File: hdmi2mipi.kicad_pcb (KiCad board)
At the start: 4 copper layers, 55 x 55 mm, 166 parts, among them J1 USB_C_Receptacle_USB2.0, J2 HDMI_A_1.4, J4 TP, J5 QWIIC, J6 BOOT, J7 SWD, J8 AudioJack3, J9 QWIIC, Q1 BC846, Q2 BC846, Q3 BC846, Q4 BC846, Q5 BC846, Q6 BC846, Q7 2SC2712, U1 SY8079AAC, U10 SY8079AAC, U11 SY8079AAC, U3 SY6280AAC, U4 PCA9306DC, U5 W25Q16JVUXIQ, U6 W25Q16JVUXIQ, U7 RP2040, U8 MS4344, U9 SY8079AAC, X1 SG-210STF, Y1 12MHz

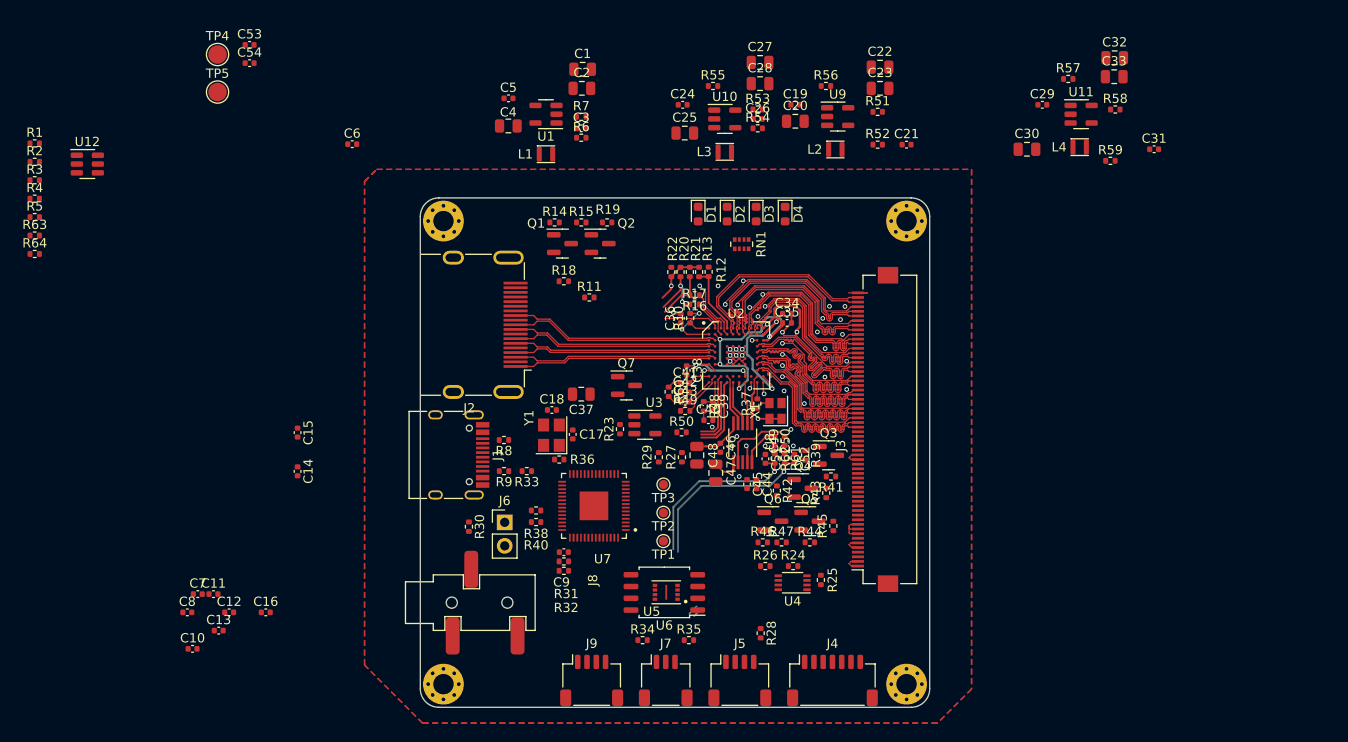
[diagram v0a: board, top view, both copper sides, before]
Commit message: Simplify and get ready for component placement and routing
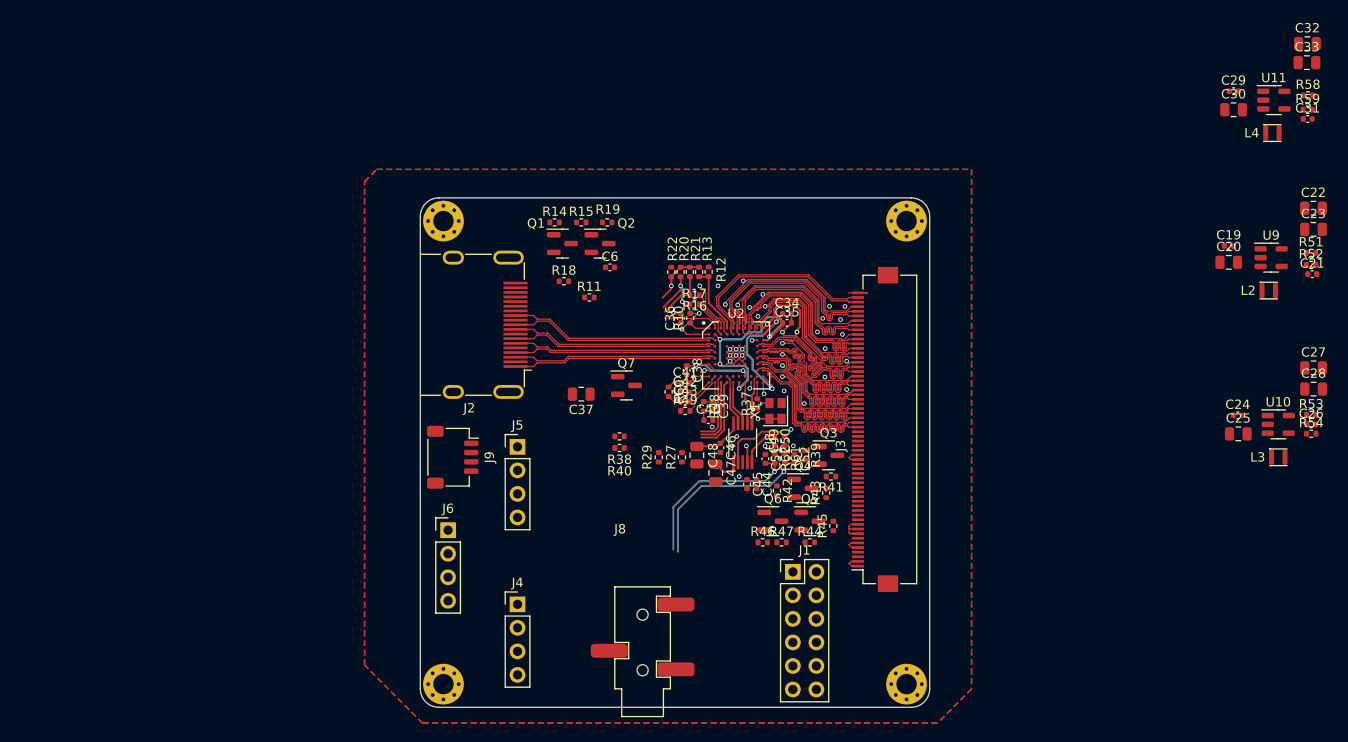
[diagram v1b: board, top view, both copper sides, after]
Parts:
- removed C1, C2, C4: 22u, Capacitor_SMD:C_0805_2012Metric
- removed C10, C12, C13, C14, C15, C16, C5, C7, C9: 100n, Capacitor_SMD:C_0402_1005Metric
- removed C11, C8: 1u, Capacitor_SMD:C_0402_1005Metric
- removed C17, C18, C3: 22p, Capacitor_SMD:C_0402_1005Metric
- removed C53: 2.2u, Capacitor_SMD:C_0402_1005Metric
- removed C54: ~, Capacitor_SMD:C_0402_1005Metric
- removed D1, D2, D3, D4: LED, LED_SMD:LED_0603_1608Metric
- removed J7: SWD, Connector_JST:JST_SH_SM03B-SRSS-TB_1x03-1MP_P1.00mm_Horizontal
- removed L1: 2.2u, custom:Inductor_MSC20FC
- removed R1, R50, R55, R56, R57, R7: 10k, Resistor_SMD:R_0402_1005Metric
- removed R2: 0, Resistor_SMD:R_0402_1005Metric
- removed R23, R24, R25, R26, R28: 4.7k, Resistor_SMD:R_0402_1005Metric
- removed R3, R4: 10, Resistor_SMD:R_0402_1005Metric
- removed R30, R33, R36: 1k, Resistor_SMD:R_0402_1005Metric
- removed R31, R32: 27, Resistor_SMD:R_0402_1005Metric
- removed R34, R35: 100, Resistor_SMD:R_0402_1005Metric
- removed R5: 6.8k, Resistor_SMD:R_0402_1005Metric
- removed R6: 45.3k, Resistor_SMD:R_0402_1005Metric
- removed R63: 50k, Resistor_SMD:R_0402_1005Metric
- removed R64: 100k, Resistor_SMD:R_0402_1005Metric
- removed R8, R9: 5.1k, Resistor_SMD:R_0402_1005Metric
- removed RN1: 1K, Resistor_SMD:R_Array_Convex_4x0402
- removed TP1, TP2, TP3: TestPoint, TestPoint:TestPoint_Pad_D1.0mm
- removed TP4, TP5: TestPoint, TestPoint:TestPoint_Pad_D2.0mm
- removed U1: SY8079AAC, Package_TO_SOT_SMD:SOT-23-5
- removed U12: ~, Package_TO_SOT_SMD:SOT-23-6
- removed U3: SY6280AAC, Package_TO_SOT_SMD:SOT-23-5
- removed U4: PCA9306DC, Package_SO:VSSOP-8_2.3x2mm_P0.5mm
- removed U5: W25Q16JVUXIQ, custom:PSON50P300X200X60-9N
- removed U6: W25Q16JVUXIQ, Package_SO:SOIC-8_5.23x5.23mm_P1.27mm
- removed U7: RP2040, custom:QFN40P700X700X90-57N
- removed Y1: 12MHz, Crystal:Crystal_SMD_3225-4Pin_3.2x2.5mm
- C6: value ~ -> 0.1u
- J1: value USB_C_Receptacle_USB2.0 -> IO; footprint Connector_USB:USB_C_Receptacle_HRO_TYPE-C-31-M-12 -> Connector_PinHeader_2.54mm:PinHeader_2x06_P2.54mm_Vertical
- J4: value TP -> Conn_01x04; footprint Connector_JST:JST_SH_SM07B-SRSS-TB_1x07-1MP_P1.00mm_Horizontal -> Connector_PinHeader_2.54mm:PinHeader_1x04_P2.54mm_Vertical
- J5: value QWIIC -> Conn_01x04; footprint Connector_JST:JST_SH_SM04B-SRSS-TB_1x04-1MP_P1.00mm_Horizontal -> Connector_PinHeader_2.54mm:PinHeader_1x04_P2.54mm_Vertical
- J6: value BOOT -> Conn_01x03; footprint Connector_PinHeader_2.54mm:PinHeader_1x02_P2.54mm_Vertical -> Connector_PinHeader_2.54mm:PinHeader_1x04_P2.54mm_Vertical
- moved C24 68.7 mm to (60.8, -4.02)
- moved C27 68.3 mm to (68.9, -9.15)
- moved C28 68.3 mm to (68.9, -6.86)
- moved C26 68.3 mm to (68.7, -3.05)
- moved L3 68.3 mm to (65.1, 0.51)
- moved R53 68.3 mm to (68.7, -4.07)
- moved R54 68.3 mm to (68.7, -2.03)
- moved U10 68.3 mm to (65.1, -3.05)
- moved C25 68.0 mm to (60.8, -2.02)
- moved L2 49.2 mm to (64.1, -17.5)
- moved C19 49.2 mm to (59.8, -22.3)
- moved C20 49.2 mm to (59.8, -20.5)
- moved C22 49.2 mm to (68.9, -26.4)
- moved C23 49.2 mm to (68.9, -24.1)
- moved R51 49.2 mm to (68.7, -21.6)
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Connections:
- C19 pad 1: VBUS -> 3V3_HDMI
- C20 pad 1: VBUS -> 3V3_HDMI
- C24 pad 1: VBUS -> 3V3_HDMI
- C25 pad 1: VBUS -> 3V3_HDMI
- C29 pad 1: VBUS -> 3V3_HDMI
- C30 pad 1: VBUS -> 3V3_HDMI
- C44 pad 1: +3V3 -> 3V3_HDMI
- C45 pad 1: +3V3 -> 3V3_HDMI
- J3 pad 1: Net-(J3-FB1-Pad1) -> Net-(J1-Pin_4)
- J3 pad 10: Net-(D5-K) -> Net-(J1-Pin_8)
- J3 pad 13: Net-(J3-5.8v-VEE) -> Net-(J1-Pin_10)
- J3 pad 14: Net-(J3-5.8v-VDD) -> Net-(J1-Pin_12)
- J3 pad 2: Net-(J3-FB1-Pad1) -> Net-(J1-Pin_4)
- J3 pad 5: Net-(J3-FB2-Pad5) -> Net-(J1-Pin_6)
- J3 pad 6: Net-(J3-FB2-Pad5) -> Net-(J1-Pin_6)
- J3 pad 8: Net-(D5-K) -> Net-(J1-Pin_8)
- J3 pad 9: Net-(D5-K) -> Net-(J1-Pin_8)
- J4 pad 1: TP_INT -> GND
- J4 pad 2: TP_RST -> +1V1
- J4 pad 3: Net-(J4-Pin_3) -> +1V2
- J4 pad 4: Net-(J4-Pin_4) -> +1V8
- J5 pad 2: +3V3 -> 3V3_HDMI
- J6 pad 1: GND -> Net-(J6-Pin_1)
- J6 pad 2: /RP_BTN -> Net-(J6-Pin_2)
- J9 pad 2: +3V3 -> 3V3_HDMI
- J9 pad 3: Net-(J9-Pin_3) -> Net-(J5-Pin_3)
- J9 pad 4: Net-(J9-Pin_4) -> Net-(J5-Pin_4)
- R27 pad 2: Net-(J9-Pin_4) -> Net-(J5-Pin_4)
- R29 pad 2: Net-(J9-Pin_3) -> Net-(J5-Pin_3)
- R38 pad 1: Net-(U2-~{RESET}) -> 3V3_HDMI
- R38 pad 2: GND -> Net-(J6-Pin_2)
- R40 pad 1: Net-(U2-INT) -> Net-(J6-Pin_1)
- U10 pad 1: 1V1_EN -> 3V3_HDMI
- U10 pad 4: VBUS -> 3V3_HDMI
- U11 pad 1: 1V8_EN -> 3V3_HDMI
- U11 pad 4: VBUS -> 3V3_HDMI
- U2 pad J3: Net-(U2-INT) -> Net-(J6-Pin_1)
- U2 pad K3: Net-(J9-Pin_3) -> Net-(J5-Pin_3)
- U2 pad K4: Net-(J9-Pin_4) -> Net-(J5-Pin_4)
- U2 pad K8: Net-(U2-~{RESET}) -> Net-(J6-Pin_2)
- U8 pad 9: +3V3 -> 3V3_HDMI
- U9 pad 1: 1V2_EN -> 3V3_HDMI
- U9 pad 4: VBUS -> 3V3_HDMI
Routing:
- net Net-(J9-Pin_4): track 8.08 -> 0.00 mm
- net Net-(J5-Pin_4): track 0.00 -> 8.08 mm
- net Net-(U2-INT): track 7.68 -> 0.00 mm
- net Net-(J6-Pin_1): track 0.00 -> 7.68 mm
- net Net-(J9-Pin_3): track 7.41 -> 0.00 mm
- net Net-(J5-Pin_3): track 0.00 -> 7.41 mm
- net Net-(J1-Pin_8): track 0.00 -> 3.77 mm
- net Net-(D5-K): track 3.77 -> 0.00 mm
- net Net-(J3-FB2-Pad5): track 2.12 -> 0.00 mm
- net Net-(J3-FB1-Pad1): track 2.12 -> 0.00 mm
- net Net-(J1-Pin_6): track 0.00 -> 2.12 mm
- net Net-(J1-Pin_4): track 0.00 -> 2.12 mm
- net +3V3: track 1.81 -> 0.00 mm, vias 1 -> 0
- net 3V3_HDMI: track 21.8 -> 23.6 mm, vias 5 -> 6
- net /AUDIO_L: track 20.8 -> 19.7 mm
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- added copper zone on In2.Cu, net 3V3_HDMI
- removed copper zone on In2.Cu, net +3V3

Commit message: tracing done
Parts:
- moved C33 86.3 mm to (1.20, 12.2), turned to -90 degrees
- moved C32 82.4 mm to (6.20, 9.98), turned to -90 degrees
- moved C28 79.5 mm to (-9.72, 4.44), turned to 90 degrees
- moved C30 78.5 mm to (-0.84, 12.2), turned to -90 degrees
- moved C27 77.8 mm to (-7.69, 4.44), turned to 90 degrees
- moved L4 77.0 mm to (0.47, 8.36), turned to 90 degrees
- moved U11 77.0 mm to (3.21, 8.33), turned to -90 degrees
- moved R59 76.9 mm to (5.45, 7.20), turned to -90 degrees
- moved R58 76.2 mm to (7.43, 7.19), turned to 90 degrees
- moved C31 75.5 mm to (6.44, 7.17), turned to -90 degrees
- moved R54 75.3 mm to (-6.14, 5.90), turned to -90 degrees
- moved C23 75.0 mm to (6.08, 16.9), turned to -90 degrees
- moved C22 74.7 mm to (8.11, 16.9), turned to -90 degrees
- moved C26 74.4 mm to (-5.12, 5.90), turned to -90 degrees
- moved L3 74.1 mm to (-7.97, 12.7), turned to 90 degrees
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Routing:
- net 3V3_HDMI: track 23.6 -> 168.8 mm, vias 6 -> 8
- net +1V2: track 15.4 -> 78.6 mm, vias 2 -> 3
- net +1V8: track 0.00 -> 54.7 mm, vias 0 -> 2
- net +1V1: track 24.3 -> 74.9 mm, vias 4 -> 5
- net Net-(J6-Pin_2): track 0.77 -> 42.1 mm
- net Net-(J6-Pin_1): track 7.68 -> 42.5 mm, vias 0 -> 1
- net Net-(J5-Pin_4): track 8.08 -> 41.6 mm
- net Net-(J5-Pin_3): track 7.41 -> 38.9 mm
- net 3V3_S2: track 0.00 -> 28.3 mm, vias 0 -> 1
- net Net-(J2-HPD/HEAC-): track 0.00 -> 27.3 mm
- net Net-(J1-Pin_12): track 0.00 -> 23.7 mm
- net 3V3_S1: track 0.00 -> 22.1 mm, vias 0 -> 1
- net Net-(J1-Pin_10): track 0.00 -> 20.3 mm
- net Net-(J3-1.8-S1): track 0.00 -> 17.0 mm
- net Net-(J2-CEC): track 6.09 -> 23.0 mm
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
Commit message: tracing done
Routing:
- net Net-(J1-Pin_12): track 23.7 -> 27.5 mm
- net Net-(J1-Pin_8): track 18.5 -> 21.3 mm
- net Net-(J1-Pin_10): track 20.3 -> 22.7 mm
- net Net-(J1-Pin_4): track 7.07 -> 8.42 mm
- net Net-(J1-Pin_6): track 12.3 -> 13.5 mm
- net 1V8_S1: track 12.5 -> 11.6 mm
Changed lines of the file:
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@@
+	)
+	(segment
+		(start 14.6 8.490684)
+		(end 14.6 10.28)
+		(width 0.2)
+		(layer "F.Cu")
+		(net 54)
 	)
 	(segment
@@
 	)
 	(segment
-		(start 14.6 8.490684)
-		(end 14.6 10.28)
-		(width 0.2)
-		(layer "F.Cu")
-		(net 54)
-	)
-	(segment
-		(start 14.6 10.28)
-		(end 14.188 10.692)
-		(width 0.2)
-		(layer "F.Cu")
-		(net 54)
-	)
-	(segment
-		(start 14.188 16.492)
-		(end 12.725 17.955)
-		(width 0.2)
-		(layer "F.Cu")
-		(net 54)
-	)
-	(segment
 		(start 14.05 7.239316)
 		(end 14.05 7.29)
@@
 	)
 	(segment
+		(start 14.6 10.28)
+		(end 14.02 10.86)
+		(width 0.2)
+		(layer "F.Cu")
+		(net 54)
+	)
+	(segment
+		(start 14.02 10.86)
+		(end 14.02 16.66)
+		(width 0.2)
+		(layer "F.Cu")
+		(net 54)
+	)
+	(segment
 		(start 14.05 7.29)
 		(end 14.100684 7.29)
@@
 	)
 	(segment
+		(start 14.950684 8.14)
+		(end 14.6 8.490684)
+		(width 0.2)
+		(layer "F.Cu")
+		(net 54)
+	)
+	(segment
 		(start 16.85 8.14)
 		(end 17.02 8.31)
@@
 	)
 	(segment
-		(start 14.950684 8.14)
-		(end 14.6 8.490684)
-		(width 0.2)
-		(layer "F.Cu")
-		(net 54)
-	)
-	(segment
-		(start 14.188 10.692)
-		(end 14.188 16.492)
-		(width 0.2)
-		(layer "F.Cu")
-		(net 54)
-	)
-	(segment
 		(start 14.100684 7.29)
 		(end 14.950684 8.14)
@@
 	)
 	(segment
+		(start 14.02 16.66)
+		(end 12.725 17.955)
+		(width 0.2)
+		(layer "F.Cu")
+		(net 54)
+	)
+	(segment
 		(start 9.44 6.265)
 		(end 9.631 6.456)
@@
 	)
 	(segment
-		(start 9.631 6.805816)
-		(end 13.861 11.035816)
+		(start 11.19 8.56)
+		(end 11.19 13.88)
 		(width 0.2)
 		(layer "F.Cu")
@@
 	)
 	(segment
-		(start 13.861 11.035816)
-		(end 13.861 14.279)
+		(start 9.631 6.456)
+		(end 9.631 7.001)
 		(width 0.2)
 		(layer "F.Cu")
@@
 	)
 	(segment
-		(start 13.861 14.279)
+		(start 11.19 13.88)
 		(end 12.725 15.415)
 		(width 0.2)
@@
 	)
 	(segment
-		(start 9.631 6.456)
-		(end 9.631 6.805816)
+		(start 9.631 7.001)
+		(end 11.19 8.56)
 		(width 0.2)
 		(layer "F.Cu")
@@
 	)
 	(segment
+		(start 24.46 18.97)
+		(end 17.855 25.575)
+		(width 0.2)
+		(layer "F.Cu")
+		(net 99)
+	)
+	(segment
 		(start 19.75 5.75)
-		(end 20.6 5.75)
+		(end 20.504 5.75)
 		(width 0.2)
 		(layer "F.Cu")
@@
 	)
 	(segment
-		(start 21.5975 6.7475)
-		(end 21.5975 19.2425)
+		(start 20.504 5.75)
+		(end 24.46 9.706)
 		(width 0.2)
 		(layer "F.Cu")
@@
 	)
 	(segment
-		(start 21.5975 19.2425)
+		(start 17.855 25.575)
 		(end 15.265 25.575)
 		(width 0.2)
@@
 	)
 	(segment
-		(start 20.6 5.75)
-		(end 21.5975 6.7475)
+		(start 24.46 9.706)
+		(end 24.46 18.97)
 		(width 0.2)
 		(layer "F.Cu")
@@
 	)
 	(segment
-		(start 20.646 7.75)
-		(end 20.72 7.824)
-		(width 0.127)
+		(start 21.14 8.752)
+		(end 21.14 19.5)
+		(width 0.2)
 		(layer "F.Cu")
 		(net 100)
 	)
 	(segment
-		(start 20.98 14.78)
-		(end 15.265 20.495)
-		(width 0.127)
+		(start 20.72 8.02)
+		(end 20.72 8.332)
+		(width 0.2)
 		(layer "F.Cu")
 		(net 100)
 	)
 	(segment
-		(start 20.72 8.586)
-		(end 20.556 8.75)
-		(width 0.127)
+		(start 20.72 8.47)
+		(end 20.44 8.75)
+		(width 0.2)
 		(layer "F.Cu")
 		(net 100)
 	)
 	(segment
-		(start 19.762 7.75)
-		(end 20.646 7.75)
-		(width 0.127)
+		(start 20.638 8.25)
+		(end 21.14 8.752)
+		(width 0.2)
+		(layer "F.Cu")
+		(net 100)
+	)
+	(segment
+		(start 20.45 7.75)
+		(end 20.72 8.02)
+		(width 0.2)
+		(layer "F.Cu")
+		(net 100)
+	)
+	(segment
+		(start 20.44 8.75)
+		(end 19.762 8.75)
+		(width 0.2)
 		(layer "F.Cu")
 		(net 100)
@@
 	)
 	(segment
-		(start 20.638 8.25)
-		(end 20.98 8.592)
-		(width 0.127)
+		(start 19.762 7.75)
+		(end 20.45 7.75)
+		(width 0.2)
 		(layer "F.Cu")
 		(net 100)
 	)
 	(segment
-		(start 20.72 8.332)
-		(end 20.72 8.586)
-		(width 0.127)
+		(start 20.145 20.495)
+		(end 15.265 20.495)
+		(width 0.2)
 		(layer "F.Cu")
 		(net 100)
 	)
 	(segment
-		(start 20.72 7.824)
-		(end 20.72 8.332)
-		(width 0.127)
-		(layer "F.Cu")
-		(net 100)
-	)
-	(segment
-		(start 20.556 8.75)
-		(end 19.762 8.75)
-		(width 0.127)
+		(start 21.14 19.5)
+		(end 20.145 20.495)
+		(width 0.2)
 		(layer "F.Cu")
 		(net 100)
@@
 		(start 19.762 8.25)
 		(end 20.638 8.25)
-		(width 0.127)
+		(width 0.2)
 		(layer "F.Cu")
 		(net 100)
 	)
 	(segment
-		(start 20.98 8.592)
-		(end 20.98 14.78)
-		(width 0.127)
+		(start 20.72 8.332)
+		(end 20.72 8.47)
+		(width 0.2)
 		(layer "F.Cu")
 		(net 100)
+	)
+	(segment
+		(start 20.504 6.25)
+		(end 21.59 7.336)
+		(width 0.2)
+		(layer "F.Cu")
+		(net 101)
+	)
+	(segment
+		(start 21.59 7.336)
+		(end 21.59 20.34)
+		(width 0.2)
+		(layer "F.Cu")
+		(net 101)
+	)
+	(segment
+		(start 21.59 20.34)
+		(end 18.895 23.035)
+		(width 0.2)
+		(layer "F.Cu")
+		(net 101)
 	)
 	(segment
@@
 	)
 	(segment
-		(start 20.504 6.25)
-		(end 21.2705 7.0165)
+		(start 18.895 23.035)
+		(end 15.265 23.035)
 		(width 0.2)
 		(layer "F.Cu")
@@
 	)
 	(segment
-		(start 21.2705 17.0295)
-		(end 15.265 23.035)
-		(width 0.2)
-		(layer "F.Cu")
-		(net 101)
-	)
-	(segment
-		(start 21.2705 7.0165)
-		(end 21.2705 17.0295)
-		(width 0.2)
-		(layer "F.Cu")
-		(net 101)
-	)
-	(segment
-		(start 18.702 11.978)
-		(end 15.265 15.415)
-		(width 0.127)
-		(layer "F.Cu")
-		(net 102)
-	)
-	(segment
-		(start 18.792 11.978)
-		(end 18.702 11.978)
-		(width 0.127)
+		(start 18.792 14.278)
+		(end 17.655 15.415)
+		(width 0.2)
 		(layer "F.Cu")
 		(net 102)
@@
 		(start 19.75 11.75)
 		(end 19.02 11.75)
-		(width 0.127)
+		(width 0.2)
 		(layer "F.Cu")
 		(net 102)
@@
 		(start 19.064 12.25)
 		(end 19.75 12.25)
-		(width 0.127)
+		(width 0.2)
+		(layer "F.Cu")
+		(net 102)
+	)
+	(segment
+		(start 18.792 11.978)
+		(end 18.792 14.278)
+		(width 0.2)
+		(layer "F.Cu")
+		(net 102)
+	)
+	(segment
+		(start 17.655 15.415)
+		(end 15.265 15.415)
+		(width 0.2)
 		(layer "F.Cu")
 		(net 102)
@@
 		(start 19.02 11.75)
 		(end 18.792 11.978)
-		(width 0.127)
+		(width 0.2)
 		(layer "F.Cu")
 		(net 102)
@@
 		(start 18.792 11.978)
 		(end 19.064 12.25)
+		(width 0.2)
+		(layer "F.Cu")
+		(net 102)
+	)
+	(segment
+		(start 18.91579 17.955)
+		(end 15.265 17.955)
+		(width 0.2)
+		(layer "F.Cu")
+		(net 103)
+	)
+	(segment
+		(start 19.75 9.768)
+		(end 19.768 9.75)
 		(width 0.127)
 		(layer "F.Cu")
-		(net 102)
-	)
-	(segment
-		(start 20.726 10.054)
-		(end 20.726 12.494)
+		(net 103)
+	)
+	(segment
+		(start 19.75 10.25)
+		(end 19.75 9.768)
 		(width 0.127)
 		(layer "F.Cu")
@@
 	)
 	(segment
-		(start 20.726 10.054)
-		(end 20.53 10.25)
-		(width 0.127)
+		(start 20.726 10.472)
+		(end 20.726 16.14479)
+		(width 0.2)
 		(layer "F.Cu")
 		(net 103)
 	)
 	(segment
-		(start 20.53 10.25)
+		(start 19.75 10.25)
+		(end 20.504 10.25)
+		(width 0.2)
+		(layer "F.Cu")
+		(net 103)
+	)
+	(segment
+		(start 20.504 10.25)
+		(end 20.726 10.472)
+		(width 0.2)
+		(layer "F.Cu")
+		(net 103)
+	)
+	(segment
+		(start 19.75 10.25)
 		(end 19.768 10.25)
 		(width 0.127)
@@
 	)
 	(segment
-		(start 19.768 9.75)
-		(end 20.422 9.75)
-		(width 0.127)
+		(start 20.726 16.14479)
+		(end 18.91579 17.955)
+		(width 0.2)
 		(layer "F.Cu")
 		(net 103)
-	)
-	(segment
-		(start 20.422 9.75)
-		(end 20.726 10.054)
-		(width 0.127)
-		(layer "F.Cu")
-		(net 103)
-	)
-	(segment
-		(start 20.726 12.494)
-		(end 15.265 17.955)
-		(width 0.127)
-		(layer "F.Cu")
-		(net 103)

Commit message: labels ordering
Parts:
- moved C27 0.09 mm to (-7.62, 4.38)
- moved C28 0.09 mm to (-9.65, 4.38)
